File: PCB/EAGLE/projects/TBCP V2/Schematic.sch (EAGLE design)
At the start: 109 parts, among them J1 FP Header, J100 ADS1115, J2 12 Supply, J3 TB Header, Q1 DMP4025LK3Q-13, SW1 SWITCH-SPDT-SMD-RIGHT-ANGLE, U1 ESP32-DEVKITC, U100 TLE9201SG, U2 7805

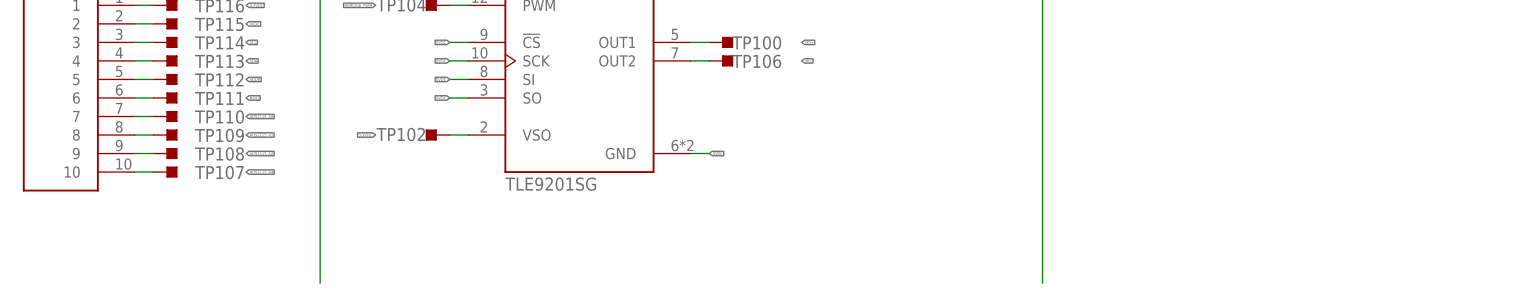
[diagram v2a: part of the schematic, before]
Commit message: TCBP 2.0 almost ready
Just need to double check for errors
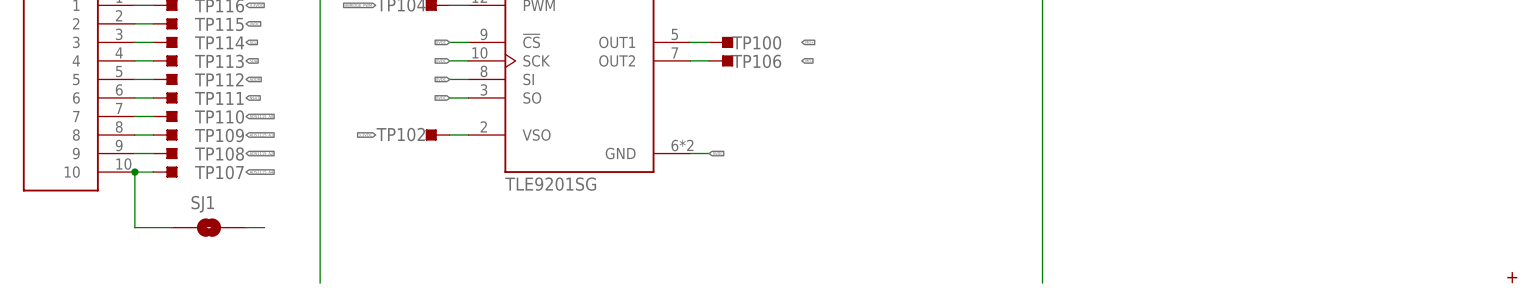
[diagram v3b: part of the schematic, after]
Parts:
- added SJ1: SOLDERJUMPERTRACE, SparkFun-Retired:SOLDERJUMPERTRACE
- added U$1: WINTEC, Wintec Logo:WINTEC
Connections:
- net 0VDC: now also SJ1.2
- net ADS1115_A4: now also SJ1.1
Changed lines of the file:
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@@
 <grid distance="0.1" unitdist="inch" unit="inch" style="lines" multiple="1" display="no" altdistance="0.01" altunitdist="inch" altunit="inch"/>
 <layers>
-<layer number="1" name="Top" color="4" fill="1" visible="no" active="no"/>
-<layer number="2" name="Route2" color="16" fill="1" visible="no" active="no"/>
-<layer number="3" name="Route3" color="17" fill="1" visible="no" active="no"/>
-<layer number="4" name="Route4" color="18" fill="1" visible="no" active="no"/>
-<layer number="5" name="Route5" color="19" fill="1" visible="no" active="no"/>
-<layer number="6" name="Route6" color="25" fill="1" visible="no" active="no"/>
-<layer number="7" name="Route7" color="26" fill="1" visible="no" active="no"/>
-<layer number="8" name="Route8" color="27" fill="1" visible="no" active="no"/>
-<layer number="9" name="Route9" color="28" fill="1" visible="no" active="no"/>
-<layer number="10" name="Route10" color="29" fill="1" visible="no" active="no"/>
-<layer number="11" name="Route11" color="30" fill="1" visible="no" active="no"/>
-<layer number="12" name="Route12" color="20" fill="1" visible="no" active="no"/>
-<layer number="13" name="Route13" color="21" fill="1" visible="no" active="no"/>
-<layer number="14" name="Route14" color="22" fill="1" visible="no" active="no"/>
-<layer number="15" name="Route15" color="23" fill="1" visible="no" active="no"/>
-<layer number="16" name="Bottom" color="1" fill="1" visible="no" active="no"/>
-<layer number="17" name="Pads" color="2" fill="1" visible="no" active="no"/>
-<layer number="18" name="Vias" color="2" fill="1" visible="no" active="no"/>
-<layer number="19" name="Unrouted" color="6" fill="1" visible="no" active="no"/>
-<layer number="20" name="Dimension" color="24" fill="1" visible="no" active="no"/>
-<layer number="21" name="tPlace" color="7" fill="1" visible="no" active="no"/>
-<layer number="22" name="bPlace" color="7" fill="1" visible="no" active="no"/>
-<layer number="23" name="tOrigins" color="15" fill="1" visible="no" active="no"/>
-<layer number="24" name="bOrigins" color="15" fill="1" visible="no" active="no"/>
-<layer number="25" name="tNames" color="7" fill="1" visible="no" active="no"/>
-<layer number="26" name="bNames" color="7" fill="1" visible="no" active="no"/>
-<layer number="27" name="tValues" color="7" fill="1" visible="no" active="no"/>
-<layer number="28" name="bValues" color="7" fill="1" visible="no" active="no"/>
+<layer number="1" name="Top" color="4" fill="1" visible="yes" active="no"/>
+<layer number="2" name="Route2" color="16" fill="1" visible="yes" active="no"/>
+<layer number="3" name="Route3" color="17" fill="1" visible="yes" active="no"/>
+<layer number="4" name="Route4" color="18" fill="1" visible="yes" active="no"/>
+<layer number="5" name="Route5" color="19" fill="1" visible="yes" active="no"/>
+<layer number="6" name="Route6" color="25" fill="1" visible="yes" active="no"/>
+<layer number="7" name="Route7" color="26" fill="1" visible="yes" active="no"/>
+<layer number="8" name="Route8" color="27" fill="1" visible="yes" active="no"/>
+<layer number="9" name="Route9" color="28" fill="1" visible="yes" active="no"/>
+<layer number="10" name="Route10" color="29" fill="1" visible="yes" active="no"/>
+<layer number="11" name="Route11" color="30" fill="1" visible="yes" active="no"/>
+<layer number="12" name="Route12" color="20" fill="1" visible="yes" active="no"/>
+<layer number="13" name="Route13" color="21" fill="1" visible="yes" active="no"/>
+<layer number="14" name="Route14" color="22" fill="1" visible="yes" active="no"/>
+<layer number="15" name="Route15" color="23" fill="1" visible="yes" active="no"/>
+<layer number="16" name="Bottom" color="1" fill="1" visible="yes" active="no"/>
+<layer number="17" name="Pads" color="2" fill="1" visible="yes" active="no"/>
+<layer number="18" name="Vias" color="2" fill="1" visible="yes" active="no"/>
+<layer number="19" name="Unrouted" color="6" fill="1" visible="yes" active="no"/>
+<layer number="20" name="Dimension" color="24" fill="1" visible="yes" active="no"/>
+<layer number="21" name="tPlace" color="7" fill="1" visible="yes" active="no"/>
+<layer number="22" name="bPlace" color="7" fill="1" visible="yes" active="no"/>
+<layer number="23" name="tOrigins" color="15" fill="1" visible="yes" active="no"/>
+<layer number="24" name="bOrigins" color="15" fill="1" visible="yes" active="no"/>
+<layer number="25" name="tNames" color="7" fill="1" visible="yes" active="no"/>
+<layer number="26" name="bNames" color="7" fill="1" visible="yes" active="no"/>
+<layer number="27" name="tValues" color="7" fill="1" visible="yes" active="no"/>
+<layer number="28" name="bValues" color="7" fill="1" visible="yes" active="no"/>
 <layer number="29" name="tStop" color="7" fill="3" visible="no" active="no"/>
 <layer number="30" name="bStop" color="7" fill="6" visible="no" active="no"/>
@@
 <layer number="35" name="tGlue" color="7" fill="4" visible="no" active="no"/>
 <layer number="36" name="bGlue" color="7" fill="5" visible="no" active="no"/>
-<layer number="37" name="tTest" color="7" fill="1" visible="no" active="no"/>
-<layer number="38" name="bTest" color="7" fill="1" visible="no" active="no"/>
+<layer number="37" name="tTest" color="7" fill="1" visible="yes" active="no"/>
+<layer number="38" name="bTest" color="7" fill="1" visible="yes" active="no"/>
 <layer number="39" name="tKeepout" color="4" fill="11" visible="no" active="no"/>
 <layer number="40" name="bKeepout" color="1" fill="11" visible="no" active="no"/>
@@
 <layer number="44" name="Drills" color="7" fill="1" visible="no" active="no"/>
 <layer number="45" name="Holes" color="7" fill="1" visible="no" active="no"/>
-<layer number="46" name="Milling" color="3" fill="1" visible="no" active="no"/>
-<layer number="47" name="Measures" color="7" fill="1" visible="no" active="no"/>
-<layer number="48" name="Document" color="7" fill="1" visible="no" active="no"/>
-<layer number="49" name="Reference" color="7" fill="1" visible="no" active="no"/>
-<layer number="50" name="dxf" color="7" fill="1" visible="no" active="no"/>
-<layer number="51" name="tDocu" color="7" fill="1" visible="no" active="no"/>
-<layer number="52" name="bDocu" color="7" fill="1" visible="no" active="no"/>
-<layer number="53" name="tGND_GNDA" color="7" fill="1" visible="no" active="no"/>
-<layer number="54" name="bGND_GNDA" color="7" fill="1" visible="no" active="no"/>
-<layer number="56" name="wert" color="7" fill="1" visible="no" active="no"/>
-<layer number="57" name="tCAD" color="7" fill="1" visible="no" active="no"/>
-<layer number="58" name="bCAD" color="11" fill="1" visible="no" active="no"/>
-<layer number="59" name="tCarbon" color="7" fill="1" visible="no" active="no"/>
-<layer number="60" name="bCarbon" color="7" fill="1" visible="no" active="no"/>
+<layer number="46" name="Milling" color="3" fill="1" visible="yes" active="no"/>
+<layer number="47" name="Measures" color="7" fill="1" visible="yes" active="no"/>
+<layer number="48" name="Document" color="7" fill="1" visible="yes" active="no"/>
+<layer number="49" name="Reference" color="7" fill="1" visible="yes" active="no"/>
+<layer number="50" name="dxf" color="7" fill="1" visible="yes" active="no"/>
+<layer number="51" name="tDocu" color="7" fill="1" visible="yes" active="no"/>
+<layer number="52" name="bDocu" color="7" fill="1" visible="yes" active="no"/>
+<layer number="53" name="tGND_GNDA" color="7" fill="1" visible="yes" active="no"/>
+<layer number="54" name="bGND_GNDA" color="7" fill="1" visible="yes" active="no"/>
+<layer number="56" name="wert" color="7" fill="1" visible="yes" active="no"/>
+<layer number="57" name="tCAD" color="7" fill="1" visible="yes" active="no"/>
+<layer number="58" name="bCAD" color="11" fill="1" visible="yes" active="no"/>
+<layer number="59" name="tCarbon" color="7" fill="1" visible="yes" active="no"/>
+<layer number="60" name="bCarbon" color="7" fill="1" visible="yes" active="no"/>
 <layer number="88" name="SimResults" color="9" fill="1" visible="yes" active="yes"/>
 <layer number="89" name="SimProbes" color="9" fill="1" visible="yes" active="yes"/>
@@
 <part name="C3" library="C0805C224J1RACTU" deviceset="C0805C224J1RACTU" device=""/>
 <part name="C2" library="C0805C224J1RACTU" deviceset="C0805C224J1RACTU" device=""/>
+<part name="SJ1" library="SparkFun-Retired" library_urn="urn:adsk.eagle:library:533" deviceset="SOLDERJUMPER" device="TRACE" package3d_urn="urn:adsk.eagle:package:41385982/1"/>
+<part name="U$1" library="Wintec Logo" deviceset="WINTEC" device=""/>
 </parts>
 <sheets>
@@
 <attribute name="VALUE" x="811.53" y="260.35" size="1.778" layer="96" rot="R90" align="center-left"/>
 </instance>
+<instance part="SJ1" gate="1" x="739.14" y="111.76" smashed="yes">
+<attribute name="NAME" x="736.6" y="114.3" size="1.778" layer="95"/>
+</instance>
+<instance part="U$1" gate="G$1" x="919.48" y="104.14" smashed="yes"/>
 </instances>
 <busses>
@@
 <junction x="721.36" y="200.66"/>
 </segment>
+<segment>
+<pinref part="SJ1" gate="1" pin="2"/>
+<wire x1="744.22" y1="111.76" x2="746.76" y2="111.76" width="0.1524" layer="91"/>
+</segment>
 </net>
 <net name="12VDC" class="0">
@@
 <label x="744.22" y="119.38" size="0.4064" layer="95" xref="yes"/>
 <pinref part="J100" gate="G$1" pin="10"/>
-</segment>
-</net>
+<wire x1="728.98" y1="119.38" x2="728.98" y2="111.76" width="0.1524" layer="91"/>
+<junction x="728.98" y="119.38"/>
+<pinref part="SJ1" gate="1" pin="1"/>
+<wire x1="728.98" y1="111.76" x2="734.06" y2="111.76" width="0.1524" layer="91"/>
+</segment>
+</net>

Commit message: TBCP 2.0 for review
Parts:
- removed SJ1: SOLDERJUMPERTRACE, SparkFun-Retired:SOLDERJUMPERTRACE
- removed SW1: SWITCH-SPDT-SMD-RIGHT-ANGLE, One_Dimensional_Pong:SWITCH-SPDT-SMD-RIGHT-ANGLE
- added S5: 500SSP1S1M6QEA, 500SSP1S1M6QEA:500SSP1S1M6QEA
- R1, R11, R2, R3, R5, R8: value (none) -> 150
- R10, R4, R7: value 8000 -> 5k
- R13, R14, R15, R16: value (none) -> 5k
- S1, S2, S3, S4: value (none) -> MOMENTARY-SWITCH-SPST-PTH-6.0MM-KIT; device SparkFun-Retired:TAC_SWITCHSMD -> SparkFun-Switches:MOMENTARY-SWITCH-SPST-PTH-6.0MM-KIT
- renumbered J100 to U4, U100 to U5
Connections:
- net 0VDC: no longer SJ1.2
- net 3.3VDC: now also S1.2, S2.2, S3.2, S4.2; no longer S1.3, S1.4, S2.3, S2.4, S3.3, S3.4, S4.3, S4.4
- net ADS1115_A4: no longer SJ1.1
- net GPIO34: no longer S3.2
- net GPIO35: no longer S4.2
- net GPIO36: no longer S1.2
- net GPIO39: no longer S2.2
- net N$1: now also S5.2; no longer SW1.S
- net N$36: now also S5.1; no longer SW1.P
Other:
- note added: "01/08/24"
- note added: "5v low dropout linear regulator with decoupling capacitors"
- note added: "BY: O.B"
- note added: "ESP32 DevKit C"
- note added: "Feedback voltage divider"
- note added: "H Bridge"
- note added: "Hardware headers / Terminals"
- note added: "LED Indicators"
- note added: "TBCP V2"
- note removed: "CHECK FOR REPLACEMENT PARTS"
- moved on the sheet: C2, C3, D1, D2, D3, D4, D5, D6, R1, R11, R2, R3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
